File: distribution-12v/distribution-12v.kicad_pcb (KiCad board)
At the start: 2 copper layers, 33 x 32 mm, 9 parts, among them J1 Conn_01x02_Socket, J3 Conn_01x02_Socket, J5 Conn_01x02_Socket

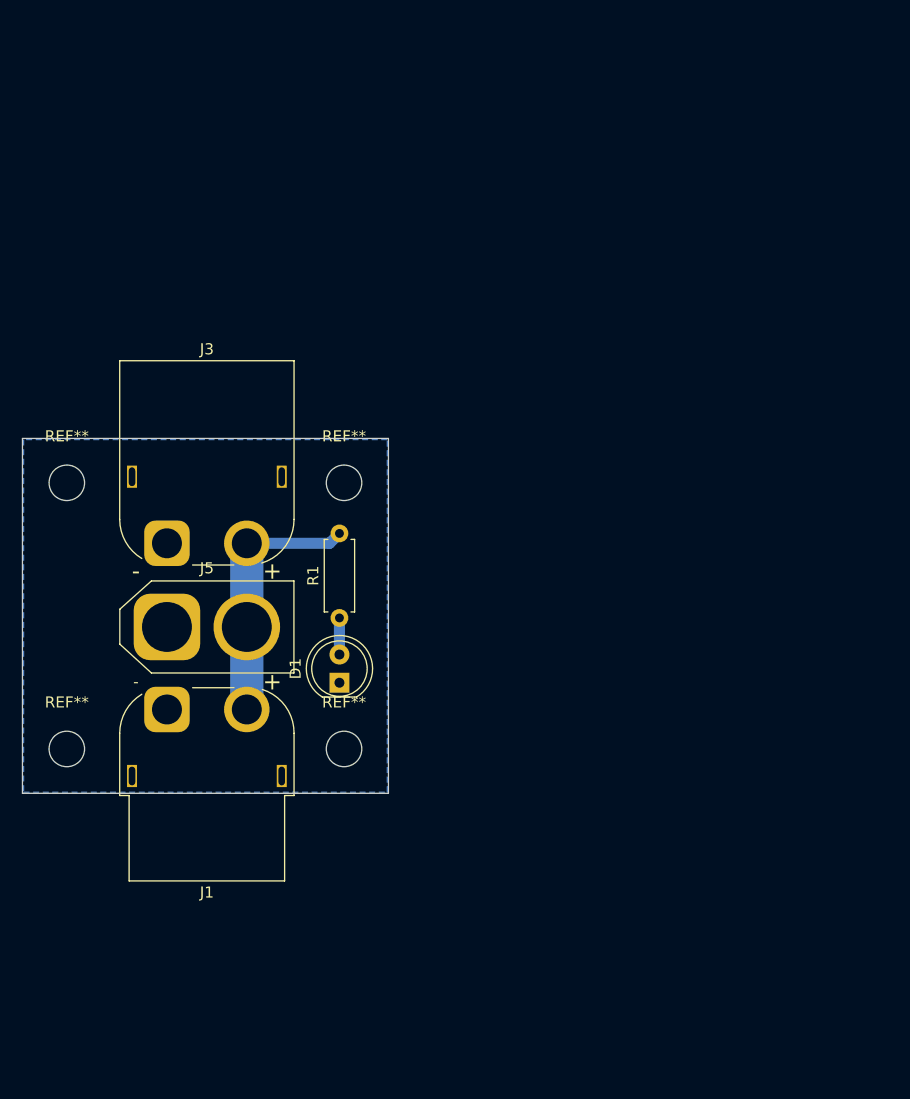
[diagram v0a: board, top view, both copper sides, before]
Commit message: change: コネクタの数を3つに増やした
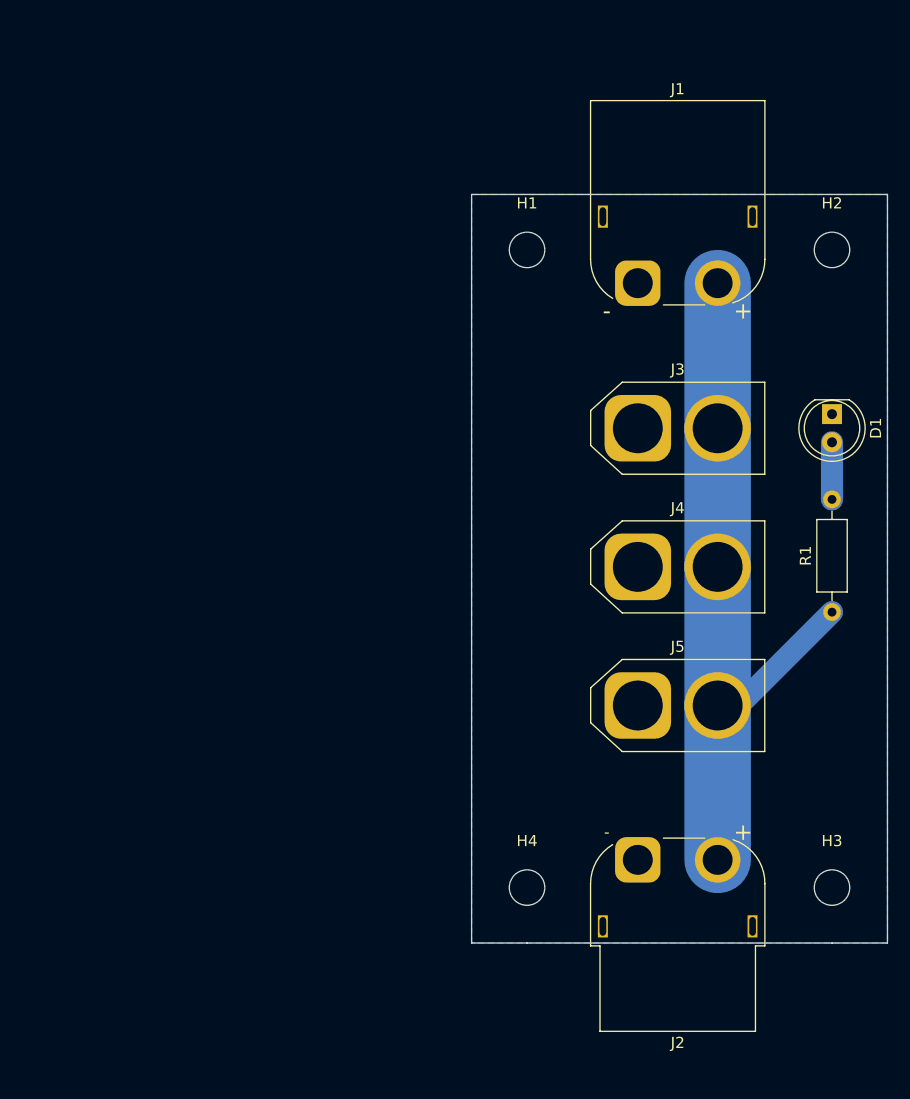
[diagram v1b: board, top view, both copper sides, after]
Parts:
- removed REF** (x4): MountingHole_3.2mm_M3, MountingHole:MountingHole_3.2mm_M3
- added H1: MountingHole, MountingHole:MountingHole_3.2mm_M3, F.Cu at (117.5, 50.0)
- added H2: MountingHole, MountingHole:MountingHole_3.2mm_M3, F.Cu at (145.0, 50.0)
- added H3: MountingHole, MountingHole:MountingHole_3.2mm_M3, F.Cu at (145.0, 107.5)
- added H4: MountingHole, MountingHole:MountingHole_3.2mm_M3, F.Cu at (117.5, 107.5)
- added J2: Conn_01x02_Socket, Connector_AMASS:AMASS_XT60PW-F_1x02_P7.20mm_Horizontal, F.Cu at (127.5, 105.0)
- added J4: Conn_01x02_Socket, Connector_AMASS:AMASS_XT60-F_1x02_P7.20mm_Vertical, F.Cu at (127.5, 78.6)
- J1: footprint Connector_AMASS:AMASS_XT60PW-F_1x02_P7.20mm_Horizontal -> Connector_AMASS:AMASS_XT60PW-M_1x02_P7.20mm_Horizontal
- J3: footprint Connector_AMASS:AMASS_XT60PW-M_1x02_P7.20mm_Horizontal -> Connector_AMASS:AMASS_XT60-F_1x02_P7.20mm_Vertical
- R1: footprint Resistor_THT:R_Axial_DIN0207_L6.3mm_D2.5mm_P7.62mm_Horizontal -> Resistor_THT:R_Axial_DIN0207_L6.3mm_D2.5mm_P10.16mm_Horizontal
- moved J1 57.3 mm to (127.5, 53.0), turned to 0 degrees
- moved D1 50.6 mm to (145.0, 64.8), turned to -90 degrees
- moved R1 44.4 mm to (145.0, 82.7)
- moved J3 43.7 mm to (127.5, 66.1)
- moved J5 43.0 mm to (127.5, 91.1)
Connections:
- net Net-(D1-K) renamed GND
- J1 pad 2: Net-(J1-Pin_2) -> +12V
- J3 pad 2: Net-(J1-Pin_2) -> +12V
- J5 pad 2: Net-(J1-Pin_2) -> +12V
- R1 pad 1: Net-(D1-A) -> +12V
- R1 pad 2: Net-(J1-Pin_2) -> Net-(D1-A)
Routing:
- net +12V: track 0.00 -> 65.8 mm
- net Net-(J1-Pin_2): track 23.7 -> 0.00 mm
- net Net-(D1-A): track 3.30 -> 5.15 mm
- added copper zone on B.Cu, net GND
- removed copper zone on B.Cu, net (none)
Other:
- board size 33 x 32 mm -> 37.5 x 67.5 mm

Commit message: fix: まるごと作り直し
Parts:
- R1: footprint Resistor_THT:R_Axial_DIN0207_L6.3mm_D2.5mm_P10.16mm_Horizontal -> Resistor_THT:R_Axial_DIN0207_L6.3mm_D2.5mm_P7.62mm_Horizontal
- moved D1 46.4 mm to (108.5, 93.5), turned to 0 degrees
- moved H1 37.8 mm to (80.0, 45.0)
- moved H4 37.6 mm to (80.0, 110.0)
- moved J1 36.8 mm to (91.0, 48.0)
- moved J3 36.8 mm to (91.0, 61.5)
- moved J5 36.6 mm to (91.0, 93.5)
- moved J2 36.5 mm to (91.0, 107.0)
- moved J4 36.5 mm to (91.0, 77.5)
- moved R1 35.8 mm to (109.5, 78.0), turned to -90 degrees
- moved H2 35.4 mm to (110.0, 45.0)
- moved H3 35.1 mm to (110.0, 110.0)
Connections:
- J1 pad : (no net) -> GND
- J2 pad : (no net) -> GND
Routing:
- net +12V: track 65.8 -> 0.00 mm
- net Net-(D1-A): track 5.15 -> 8.52 mm
- added copper zone on B.Cu, net +12V
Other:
- board size 37.5 x 67.5 mm -> 40 x 75 mm
- board text added: "※10Aまで"
- board text added: "新居浜高専"
- board text added: "配電基盤 (12V) v1"
